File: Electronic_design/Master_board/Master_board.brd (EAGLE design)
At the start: 100 x 80 mm, 23 parts

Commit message: routage
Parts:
- added 3V3, 5V_AX: 7805T, linear:TO220H
- added C1, C2: (no value), rcl:C025-024X044
- added IC1: 74LS241N, 74xx-eu:DIL20
- added MAX485: MAX481CPA, maxim:DIL08
- added R1, R2: 10K, rcl:0309/12
- added UART_AX, UART_XM: (no value), con-lstb:MA03-1
- AX: device con-lstb:MA04-1 -> con-lstb:MA03-1
- moved UART2 19.1 mm to (96.5, 14.0)
- moved UART1 11.5 mm to (96.5, 31.8)
- moved UART3 7.73 mm to (96.5, 5.08)
- moved UART5 5.24 mm to (96.5, 58.4), turned to 90 degrees
- moved AX 4.02 mm to (95.2, 73.7), turned to 0 degrees
- moved XM 4.02 mm to (94.0, 67.3), turned to 180 degrees
- moved SV6 3.81 mm to (34.3, 66.0)
- moved SV7 3.81 mm to (73.7, 62.2)
- moved SV8 3.81 mm to (36.8, 62.2)
- moved SV9 3.81 mm to (72.4, 66.0)
- moved U$3 3.81 mm to (45.7, 72.4)
- moved U$2 3.59 mm to (38.1, 26.7)
- moved UART4 1.27 mm to (96.5, 22.9)
- renumbered SV1 to ALIM_12V
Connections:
- net N$2 renamed VIN
- removed net N$113: SV9.1, U$1.GND21, U$1.GND22, U$1.GND24, U$1.GND25, U$1.GND26, U$1.GND_20
- removed net N$43: SV3.1, U$1.GND10, U$1.GND11, U$1.GND12, U$1.GND13, U$1.GND14, U$1.GND15, U$1.GND16
- removed net N$75: SV5.9, U$1.3.3V_1, U$1.3.3V_2, U$1.3.3V_3, U$1.3.3V_4, U$1.3.3V_5
- new net 12V: 5V_AX.1, U$4.P$2, XM.2
- new net 5V: R1.1, R2.1
- new net CTRL_AX: IC1.1, IC1.19, UART_AX.3
- new net CTRL_XM: MAX485.2, MAX485.3, UART_XM.3
- new net D+: MAX485.6, XM.3
- new net D-: MAX485.7, XM.4
- new net DATA_AX: AX.1, IC1.2, IC1.3, R1.2
- new net N$121: 3V3.1, U$3.P$4
- new net RX_AX: IC1.18, UART_AX.2
- new net RX_XM: MAX485.1, R2.2, UART_XM.2
- new net TX_AX: IC1.17, UART_AX.1
- new net TX_XM: MAX485.4, UART_XM.1
- new net VCC: 5V_AX.3, AX.2, C1.1, C2.1, IC1.20, MAX485.8
- net GND: now also 3V3.2, 5V_AX.2, AX.3, C1.2, C2.2, IC1.10, MAX485.5, SV3.1, SV9.1, U$1.GND10, U$1.GND11, U$1.GND12, U$1.GND13, U$1.GND14, U$1.GND15, U$1.GND16, U$1.GND21, U$1.GND22, U$1.GND24, U$1.GND25, U$1.GND26, U$1.GND_20, XM.1
- net N$1: now also 3V3.3, SV5.9, U$1.3.3V_1, U$1.3.3V_2, U$1.3.3V_3, U$1.3.3V_4, U$1.3.3V_5, U$2.P$18; no longer U$3.P$4
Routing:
- net N$1: track 0.00 -> 254.2 mm, vias 0 -> 2
- net N$20: track 0.00 -> 122.4 mm, vias 0 -> 3
- net N$21: track 0.00 -> 121.5 mm, vias 0 -> 2
- net N$11: track 0.00 -> 117.4 mm, vias 0 -> 1
- net N$18: track 0.00 -> 117.2 mm, vias 0 -> 2
- net N$19: track 0.00 -> 116.6 mm, vias 0 -> 4
- net N$4: track 0.00 -> 99.3 mm, vias 0 -> 1
- net N$10: track 0.00 -> 97.4 mm
- net VCC: track 0.00 -> 91.9 mm
- net N$7: track 0.00 -> 91.1 mm
- net N$5: track 0.00 -> 75.9 mm
- net 12V: track 0.00 -> 75.5 mm
- net DATA_AX: track 0.00 -> 74.9 mm
- net N$8: track 0.00 -> 74.0 mm
- net N$13: track 0.00 -> 71.4 mm
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- added copper zone on layer 1, net GND
- added copper zone on layer 16, net GND

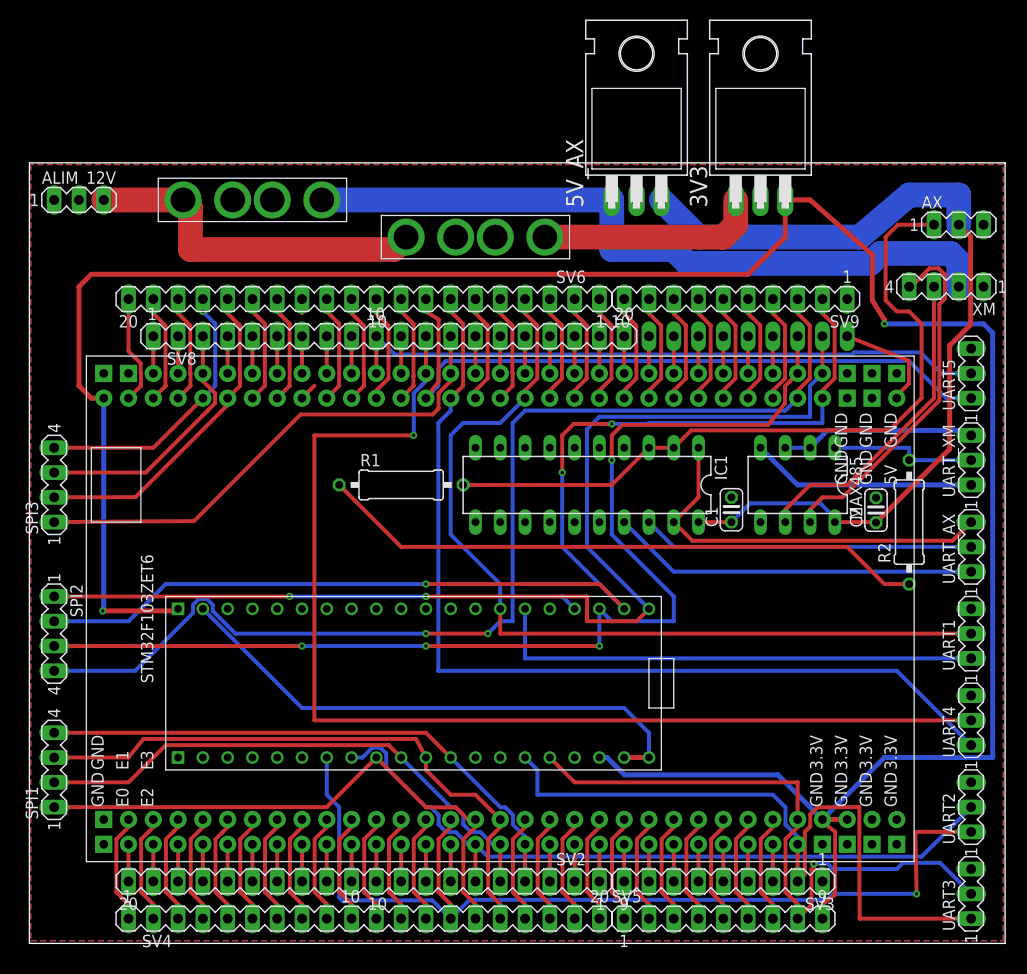
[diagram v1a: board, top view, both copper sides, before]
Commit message: DRC check OK
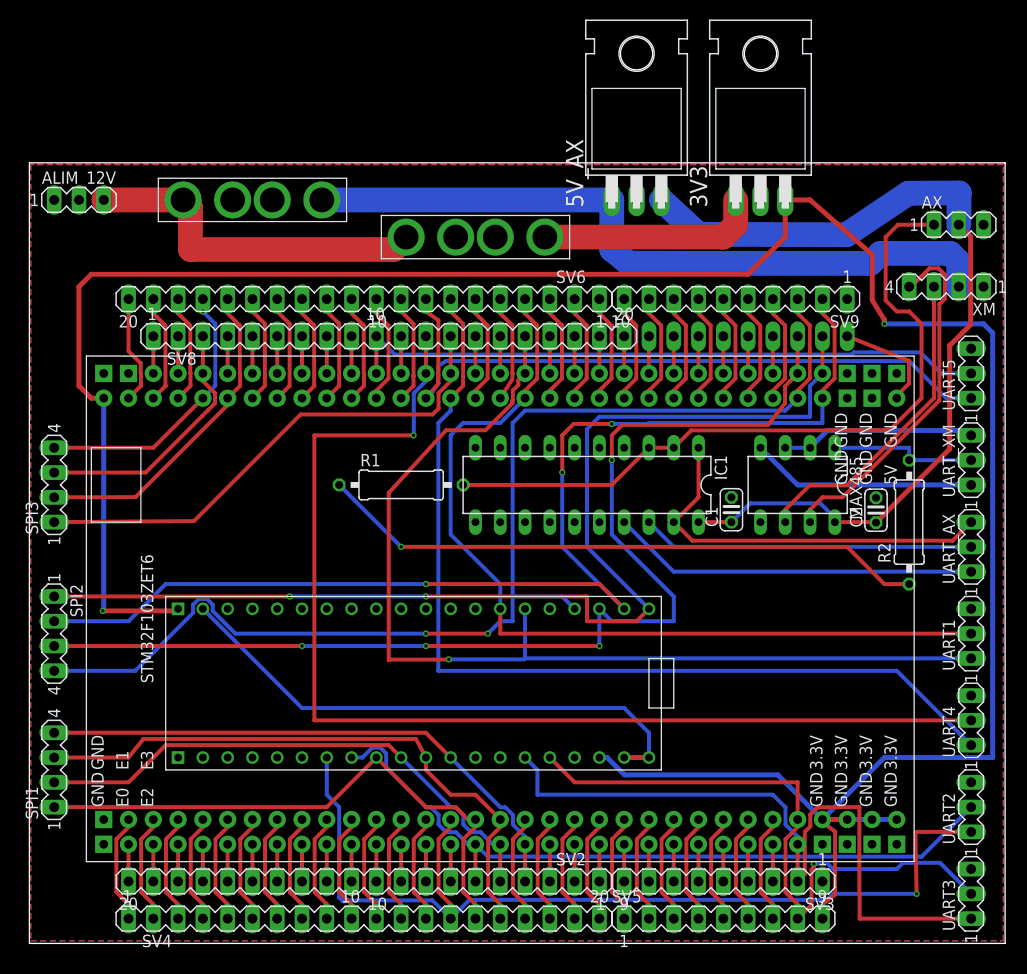
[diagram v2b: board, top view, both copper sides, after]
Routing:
- net N$28: track 54.6 -> 106.0 mm, vias 0 -> 1
- net N$85: track 3.26 -> 11.8 mm
- net N$1: track 254.2 -> 259.3 mm
- net 12V: track 75.5 -> 74.2 mm
- net N$68: track 12.5 -> 11.2 mm
- net 5V: vias 0 -> 1

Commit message: ameliorations
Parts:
- removed ALIM_12V: (no value), con-lstb:MA03-1
- added U$5: (no value), Trous_fixation:TROUS_FIXATION
- added U$6: GREEN_HEADER, PowerHeaders:GREEN_HEADER
- SPI1, SPI2, SPI3: device con-lstb:MA04-1 -> con-lstb:MA06-1
- moved SPI3 5.08 mm to (2.54, 52.1)
- moved SPI2 2.54 mm to (2.54, 34.3), turned to 90 degrees
- moved SPI1 0.13 mm to (2.67, 17.8)
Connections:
- net N$10 renamed TX4
- net N$11 renamed RX4
- net N$12 renamed RX5
- net N$13 renamed TX5
- net N$14 renamed NSS1
- net N$15 renamed SCK1
- net N$16 renamed MISO1
- net N$17 renamed MOSI1
- net N$18 renamed NSS2
- net N$19 renamed MISO2
- net N$20 renamed SCK2
- net N$21 renamed MOSI2
- net N$22 renamed NSS3
- net N$23 renamed SCK3
- net N$24 renamed MISO3
- net N$25 renamed MOSI3
- net N$28 renamed TX1
- net N$4 renamed TX2
- net N$5 renamed RX2
- net N$7 renamed RX1
- net N$8 renamed TX3
- net N$9 renamed RX3
- removed net N$1: 3V3.3, SV5.9, U$1.3.3V_1, U$1.3.3V_2, U$1.3.3V_3, U$1.3.3V_4, U$1.3.3V_5, U$2.P$18, U$2.P$40
- removed net N$3: U$2.P$19, U$2.P$20, U$2.P$39
- new net 3V3: 3V3.3, SPI1.5, SPI2.5, SPI3.5, SV5.9, U$1.3.3V_1, U$1.3.3V_2, U$1.3.3V_3, U$1.3.3V_4, U$1.3.3V_5, U$2.P$18, U$2.P$40
- net 12V: now also AX.2
- net GND: now also SPI1.6, SPI2.6, SPI3.6, U$2.P$19, U$2.P$20, U$2.P$39, U$6.P$1; no longer ALIM_12V.1
- net VCC: no longer AX.2
- net VIN: now also U$6.P$2; no longer ALIM_12V.3
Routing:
- net 3V3: track 0.00 -> 288.9 mm, vias 0 -> 2
- net N$1: track 259.3 -> 0.00 mm, vias 2 -> 0
- net N$3: track 56.1 -> 0.00 mm
- net GND: track 0.00 -> 56.1 mm
- net VIN: track 36.2 -> 44.8 mm
- net VCC: track 91.6 -> 99.8 mm, vias 0 -> 1
- net 12V: track 74.2 -> 81.4 mm
- net NSS2: track 117.2 -> 122.0 mm
- net SCK2: track 122.4 -> 126.4 mm, vias 3 -> 5
- net TX2: track 99.3 -> 103.2 mm
- net MOSI2: track 121.5 -> 118.1 mm
- net DATA_AX: track 74.9 -> 71.6 mm
- net MISO3: track 27.6 -> 25.8 mm
- net TX3: track 74.0 -> 75.8 mm
- net MOSI1: track 57.8 -> 59.1 mm
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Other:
- board text added: "12V"
- board text added: "3V3"
- board text added: "D+"
- board text added: "D-"
- board text added: "GND"
- board text added: "MISO"
- board text added: "MOSI"
- board text added: "NSS"
- board text added: "RX"
- board text added: "SCK"
- board text added: "TX"
- board text added: "Vout"
- board text added: "data"

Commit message: ajout condensateurs
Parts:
- added C3, C4: (no value), rcl:E5-10,5
- moved U$4 8.13 mm to (31.0, 76.5)
- moved U$3 0.76 mm to (45.7, 71.6)
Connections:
- net 12V: now also C3.+
- net GND: now also C3.-, C4.-
- net VIN: now also C4.+
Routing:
- net GND: track 56.1 -> 0.00 mm
- net VIN: track 44.8 -> 51.7 mm
- net 12V: track 81.4 -> 79.6 mm
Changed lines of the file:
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@@
 <elements>
 <element name="U$2" library="stm32duino boards" package="BLUEPILL" value="BLUEPILL" x="38.1" y="26.67" rot="R90"/>
-<element name="U$3" library="AUTO_FUSE" package="AUTO_FUSE" value="AUTO_FUSE" x="45.72" y="72.39"/>
+<element name="U$3" library="AUTO_FUSE" package="AUTO_FUSE" value="AUTO_FUSE" x="45.72" y="71.628"/>
 <element name="XM" library="con-lstb" library_urn="urn:adsk.eagle:library:162" package="MA04-1" package3d_urn="urn:adsk.eagle:package:8337/1" value="" x="93.98" y="67.31" rot="R180">
 <attribute name="MF" value="" x="93.98" y="67.31" size="1.778" layer="27" rot="R180" display="off"/>
@@
 <attribute name="OC_NEWARK" value="unknown" x="93.98" y="67.31" size="1.778" layer="27" rot="R180" display="off"/>
 </element>
-<element name="U$4" library="AUTO_FUSE" package="AUTO_FUSE" value="AUTO_FUSE" x="22.86" y="76.2" rot="R180"/>
+<element name="U$4" library="AUTO_FUSE" package="AUTO_FUSE" value="AUTO_FUSE" x="30.988" y="76.454" rot="R180"/>
 <element name="U$1" library="STM32F103ZET6_dev_board" package="STM32F103ZET6_DEV_BOARD" value="M32F103ZET6_DEV_BOARD" x="48.26" y="34.29" rot="R90"/>
 <element name="UART1" library="con-lstb" library_urn="urn:adsk.eagle:library:162" package="MA03-1" package3d_urn="urn:adsk.eagle:package:8339/1" value="" x="96.52" y="31.75" rot="R90">
@@
 <attribute name="OC_NEWARK" value="unknown" x="72.39" y="66.04" size="1.778" layer="27" rot="R180" display="off"/>
 </element>
-<element name="3V3" library="linear" library_urn="urn:adsk.eagle:library:262" package="TO220H" package3d_urn="urn:adsk.eagle:package:16414/1" value="7805T" x="74.93" y="86.36"/>
+<element name="3V3" library="linear" library_urn="urn:adsk.eagle:library:262" package="TO220H" package3d_urn="urn:adsk.eagle:package:16414/1" value="7805T" x="74.93" y="86.36" smashed="yes"/>
 <element name="MAX485" library="maxim" library_urn="urn:adsk.eagle:library:269" package="DIL08" package3d_urn="urn:adsk.eagle:package:17510/1" value="MAX481CPA" x="78.74" y="46.99" rot="R180">
 <attribute name="MF" value="" x="78.74" y="46.99" size="1.778" layer="27" rot="R180" display="off"/>
@@
 <attribute name="OC_NEWARK" value="unknown" x="95.25" y="73.66" size="1.778" layer="27" display="off"/>
 </element>
-<element name="5V_AX" library="linear" library_urn="urn:adsk.eagle:library:262" package="TO220H" package3d_urn="urn:adsk.eagle:package:16414/1" value="7805T" x="62.23" y="86.36"/>
+<element name="5V_AX" library="linear" library_urn="urn:adsk.eagle:library:262" package="TO220H" package3d_urn="urn:adsk.eagle:package:16414/1" value="7805T" x="62.23" y="86.36" smashed="yes"/>
 <element name="UART_XM" library="con-lstb" library_urn="urn:adsk.eagle:library:162" package="MA03-1" package3d_urn="urn:adsk.eagle:package:8339/1" value="" x="96.52" y="49.53" rot="R90">
 <attribute name="MF" value="" x="96.52" y="49.53" size="1.778" layer="27" rot="R90" display="off"/>
@@
 <attribute name="OC_NEWARK" value="unknown" x="2.54" y="34.29" size="1.778" layer="27" rot="R90" display="off"/>
 </element>
+<element name="C4" library="rcl" library_urn="urn:adsk.eagle:library:334" package="E5-10,5" package3d_urn="urn:adsk.eagle:package:23372/1" value="" x="15.748" y="73.66" rot="R90"/>
+<element name="C3" library="rcl" library_urn="urn:adsk.eagle:library:334" package="E5-10,5" package3d_urn="urn:adsk.eagle:package:23372/1" value="" x="85.725" y="75.184" rot="R340"/>
 </elements>
 <signals>
@@
 <contactref element="U$2" pad="P$20"/>
 <contactref element="U$2" pad="P$39"/>
-<wire x1="17.78" y1="34.29" x2="27.94" y2="24.13" width="0.4064" layer="16"/>
-<wire x1="27.94" y1="24.13" x2="60.96" y2="24.13" width="0.4064" layer="16"/>
-<wire x1="60.96" y1="24.13" x2="63.5" y2="21.59" width="0.4064" layer="16"/>
-<wire x1="63.5" y1="21.59" x2="63.5" y2="19.05" width="0.4064" layer="16"/>
-<wire x1="60.96" y1="19.05" x2="63.5" y2="19.05" width="0.508" layer="1"/>
+<contactref element="C4" pad="-"/>
+<contactref element="C3" pad="-"/>
 </signal>
 <signal name="TX2">
@@
 <contactref element="U$3" pad="P$4"/>
 <contactref element="3V3" pad="1"/>
-<wire x1="52.83" y1="72.39" x2="71.12" y2="72.39" width="2.54" layer="1"/>
-<wire x1="71.12" y1="72.39" x2="72.39" y2="73.66" width="2.54" layer="1"/>
+<wire x1="52.83" y1="71.628" x2="70.104" y2="71.755" width="2.54" layer="1"/>
+<wire x1="70.104" y1="71.755" x2="72.39" y2="73.66" width="2.54" layer="1"/>
 <wire x1="72.39" y1="73.66" x2="72.39" y2="76.2" width="2.54" layer="1"/>
 </signal>
@@
 <contactref element="U$4" pad="P$2"/>
 <contactref element="5V_AX" pad="1"/>
-<wire x1="29.97" y1="76.2" x2="59.69" y2="76.2" width="2.54" layer="16"/>
+<wire x1="38.098" y1="76.454" x2="59.69" y2="76.2" width="2.54" layer="16"/>
 <contactref element="AX" pad="2"/>
 <wire x1="59.69" y1="76.2" x2="59.69" y2="72.39" width="2.54" layer="16"/>
 <wire x1="59.69" y1="72.39" x2="60.96" y2="71.12" width="2.54" layer="16"/>
-<wire x1="87.249" y1="77.089" x2="94.488" y2="77.089" width="2.54" layer="16"/>
+<wire x1="84.709" y1="77.089" x2="94.488" y2="77.089" width="2.54" layer="16"/>
 <wire x1="94.488" y1="77.089" x2="95.25" y2="76.327" width="2.54" layer="16"/>
 <wire x1="95.25" y1="76.327" x2="95.25" y2="73.66" width="2.54" layer="16"/>
-<wire x1="60.96" y1="71.12" x2="81.28" y2="71.12" width="2.54" layer="16"/>
-<wire x1="81.28" y1="71.12" x2="87.249" y2="77.089" width="2.54" layer="16"/>
+<wire x1="81.28" y1="71.12" x2="60.96" y2="71.12" width="2.54" layer="16"/>
+<wire x1="81.28" y1="71.12" x2="84.709" y2="77.089" width="2.54" layer="16"/>
 <wire x1="95.25" y1="73.66" x2="95.25" y2="67.31" width="2.54" layer="16"/>
+<contactref element="C3" pad="+"/>
+<wire x1="83.338178125" y1="76.052728125" x2="81.28" y2="71.12" width="0.1524" layer="16"/>
 </signal>
 <signal name="5V">
@@
 <contactref element="U$3" pad="P$2"/>
 <contactref element="U$4" pad="P$4"/>
-<wire x1="15.75" y1="76.2" x2="16.51" y2="75.44" width="2.54" layer="1"/>
-<wire x1="16.51" y1="71.12" x2="16.51" y2="75.44" width="2.54" layer="1"/>
+<wire x1="23.878" y1="76.454" x2="23.876" y2="71.122" width="2.54" layer="1"/>
+<wire x1="16.51" y1="71.12" x2="23.876" y2="71.122" width="2.54" layer="1"/>
 <wire x1="16.51" y1="71.12" x2="37.34" y2="71.12" width="2.54" layer="1"/>
-<wire x1="37.34" y1="71.12" x2="38.61" y2="72.39" width="2.54" layer="1"/>
+<wire x1="37.34" y1="71.12" x2="38.61" y2="71.628" width="2.54" layer="1"/>
 <contactref element="U$6" pad="P$2"/>
 <wire x1="2.54" y1="76.2" x2="2.54" y2="74.93" width="2.54" layer="1"/>
@@
 <wire x1="5.08" y1="72.39" x2="15.24" y2="72.39" width="3" layer="1"/>
 <wire x1="15.24" y1="72.39" x2="16.51" y2="71.12" width="2.54" layer="1"/>
+<contactref element="C4" pad="+"/>
+<wire x1="16.51" y1="71.12" x2="15.748" y2="71.12" width="0" layer="19" extent="1-1"/>
 </signal>
 <signal name="3V3">
